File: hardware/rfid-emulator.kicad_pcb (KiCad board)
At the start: 4 copper layers, 162 x 72 mm, 94 parts, among them J1 AVR-JTAG-10, J2 Micro_USB, J3 OSTTC020162, Q1 2N3904, Q2 2N3906, Q3 2N3906, Q4 IRLML6344TRPBF, Q5 IRLML6344TRPBF, SW1 EN11-HSM1BF20, U1 NHD-C0216CiZ-FSW-FBW-3V3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

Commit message: Re-add Noelle's changes
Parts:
- added C32: 1.5n, Capacitors_SMD:C_0805_HandSoldering, F.Cu at (122.0, 81.2)

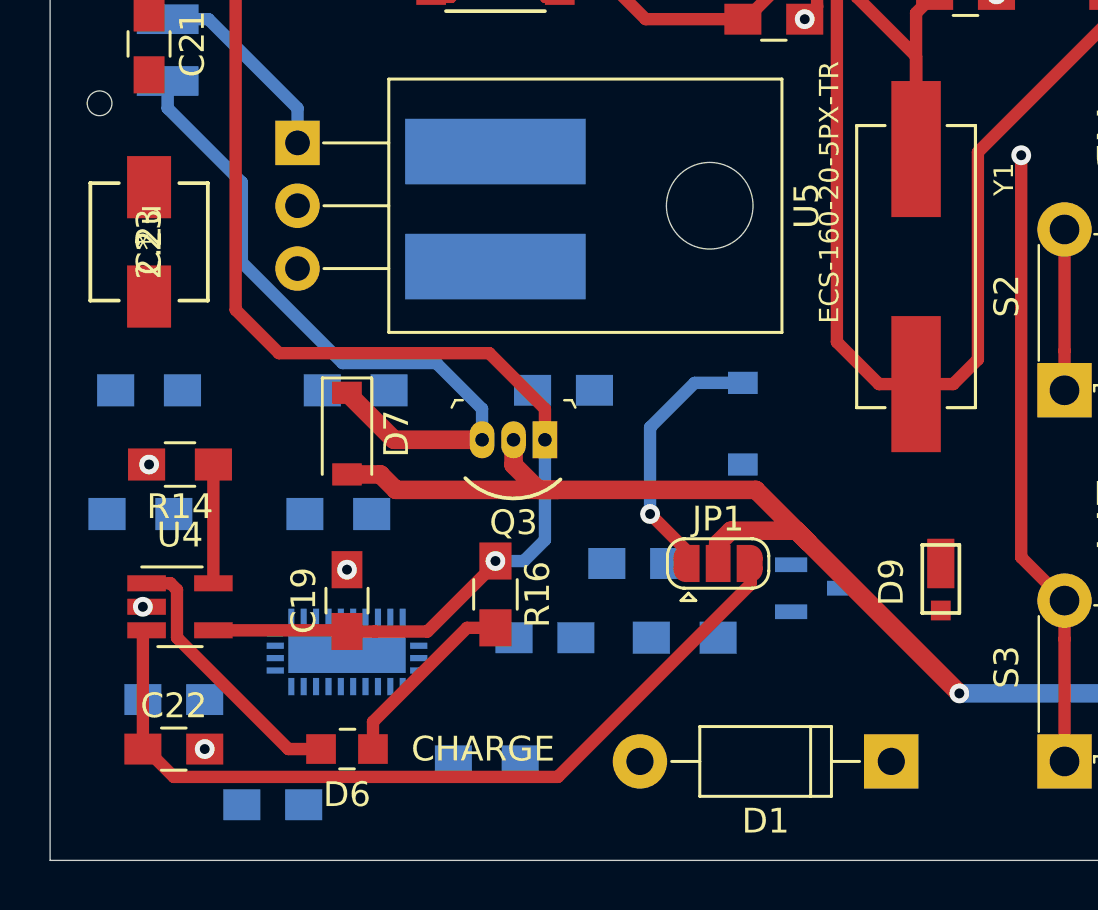
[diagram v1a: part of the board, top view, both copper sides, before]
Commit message: Ian changes rfid-emulator.kicad_pcb
Added all traces and connections associated with the battery management system.
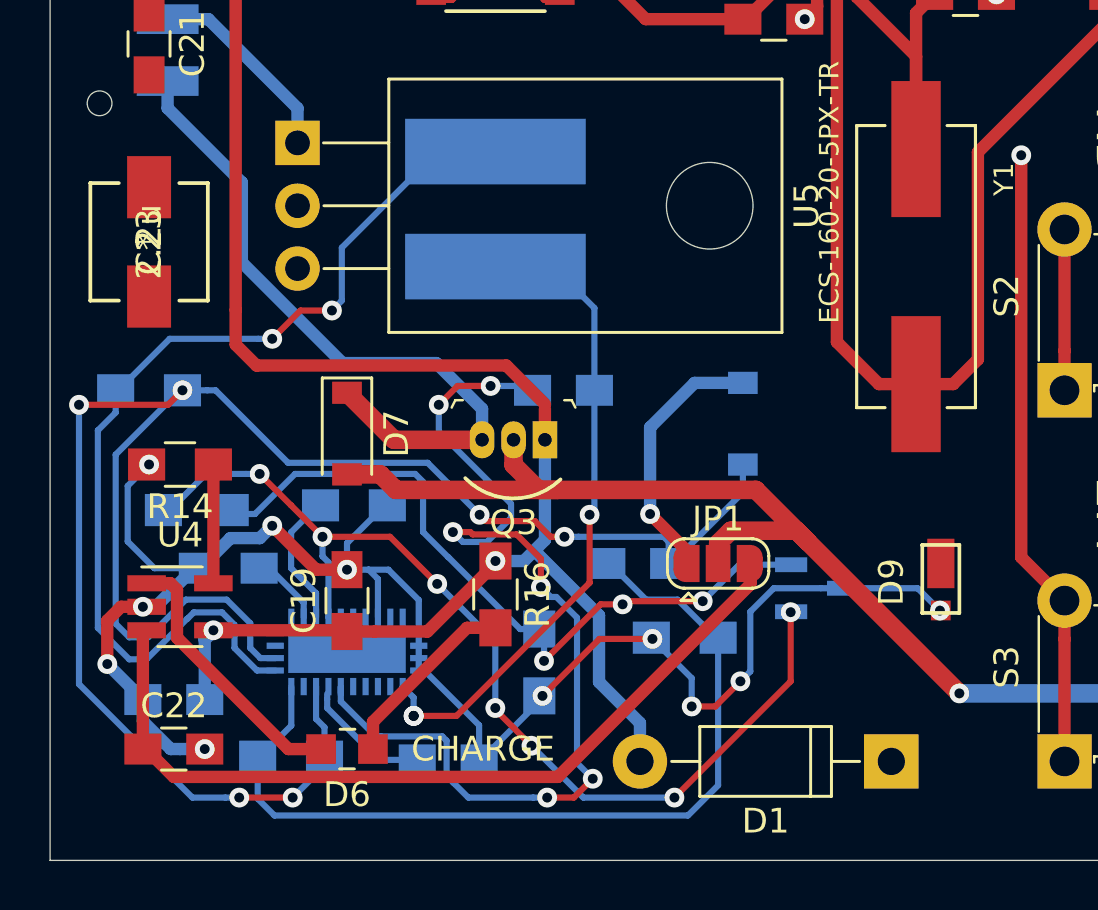
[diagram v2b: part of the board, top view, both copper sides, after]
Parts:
- moved R5 15.0 mm to (78.7, 130.8)
- moved C7 13.1 mm to (76.2, 123.2)
- moved R4 11.7 mm to (81.3, 120.7)
- moved R2 10.1 mm to (88.8, 127.0), turned to 270 degrees
- moved C6 7.32 mm to (85.1, 130.9), turned to 0 degrees
- moved R1 2.29 mm to (74.9, 120.8)
- turned C11 to 180 degrees
- turned R8 to 180 degrees
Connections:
- U2 pad 12: (no net) -> GND
- U2 pad 13: (no net) -> GND
- U2 pad 14: (no net) -> GND
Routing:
- net Net-(C11-Pad1): track 0.00 -> 79.5 mm, vias 0 -> 6
- net GND: track 24.8 -> 94.1 mm, vias 22 -> 29
- net Net-(D1-Pad1): track 0.00 -> 41.6 mm, vias 0 -> 7
- net Net-(C10-Pad1): track 0.00 -> 40.7 mm, vias 0 -> 6
- net Net-(L1-Pad1): track 0.00 -> 40.6 mm, vias 0 -> 2
- net Net-(C11-Pad2): track 0.00 -> 36.3 mm
- net Net-(R1-Pad2): track 0.00 -> 30.0 mm, vias 0 -> 3
- net Net-(C10-Pad2): track 0.00 -> 26.6 mm, vias 0 -> 3
- net /USB_VBUS: track 61.6 -> 75.8 mm, vias 1 -> 2
- net Net-(R4-Pad1): track 0.00 -> 5.49 mm
- net Net-(C6-Pad1): track 0.00 -> 5.08 mm
- net Net-(C7-Pad2): track 0.00 -> 2.97 mm

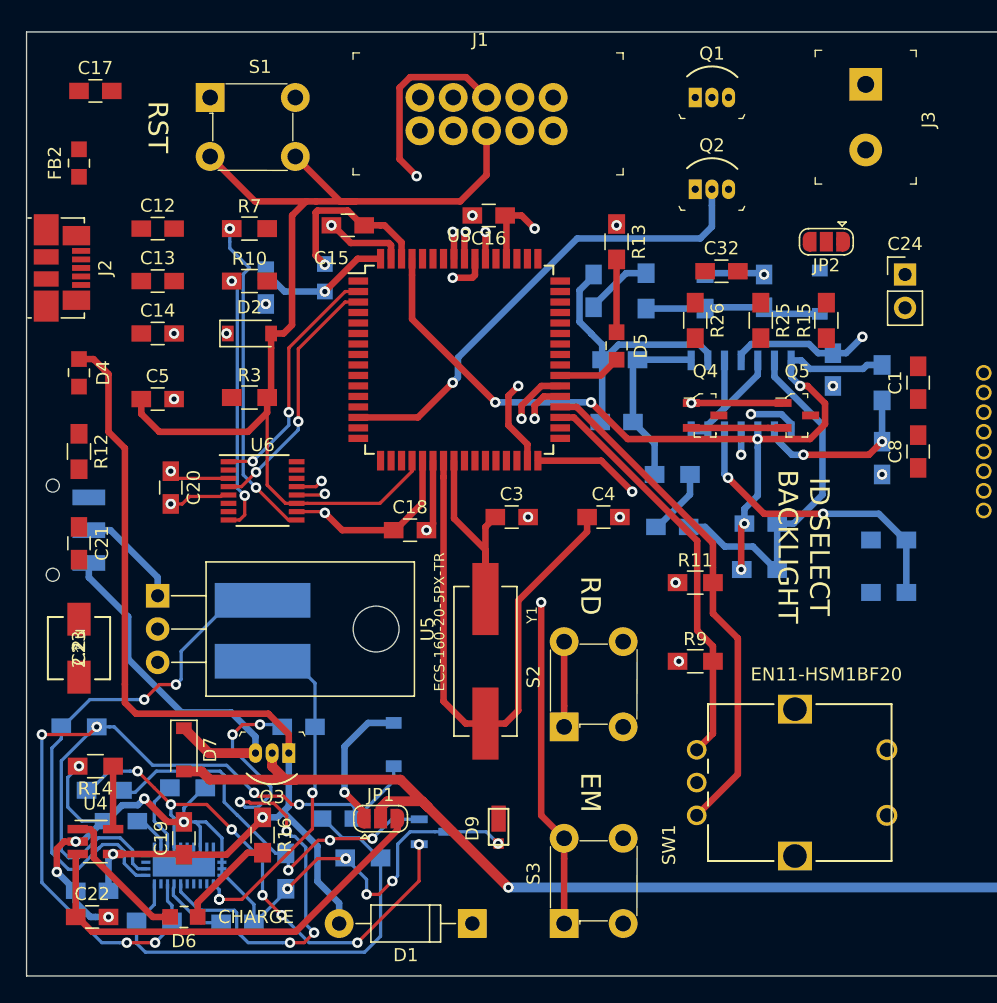
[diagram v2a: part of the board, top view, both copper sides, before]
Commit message: Delete extraneous traces and modify some problematic footprints
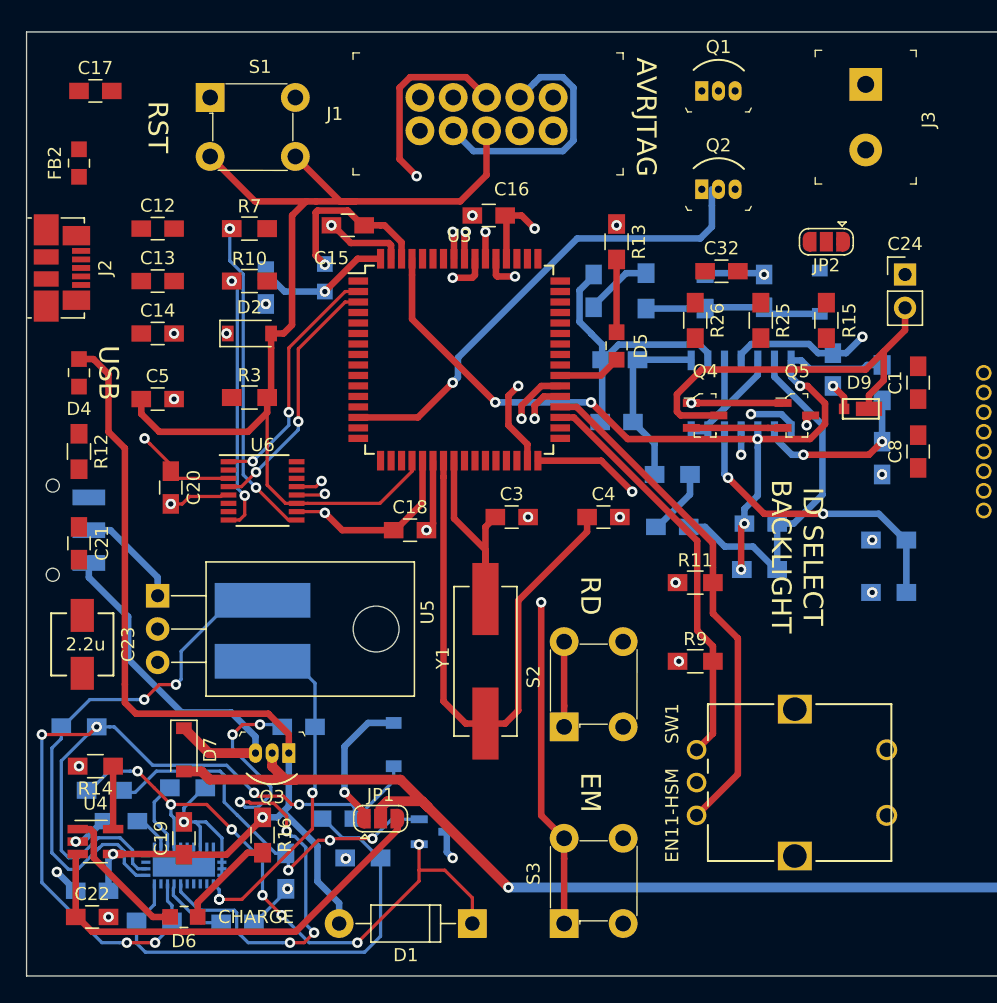
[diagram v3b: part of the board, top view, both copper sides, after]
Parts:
- SW1: value EN11-HSM1BF20 -> EN11-HSM
- moved D9 42.1 mm to (133.2, 91.8), turned to 180 degrees
- moved Q1 0.71 mm to (120.5, 67.5)
- moved SW1 0.57 mm to (127.5, 120.2)
- moved Q2 0.50 mm to (120.5, 75.0)
- moved C23 0.38 mm to (73.2, 109.7)
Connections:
- U2 pad 12: GND -> (no net)
- U2 pad 13: GND -> (no net)
- U2 pad 14: GND -> (no net)
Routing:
- net GND: track 94.1 -> 53.0 mm
- net /ANTENNA: track 0.00 -> 30.6 mm
- net +3V3: track 51.1 -> 73.6 mm, vias 10 -> 11
- net Net-(D1-Pad1): track 41.6 -> 48.5 mm
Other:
- board text added: "AVRJTAG"
- board text added: "OFF"
- board text added: "ON"
- board text added: "USB"

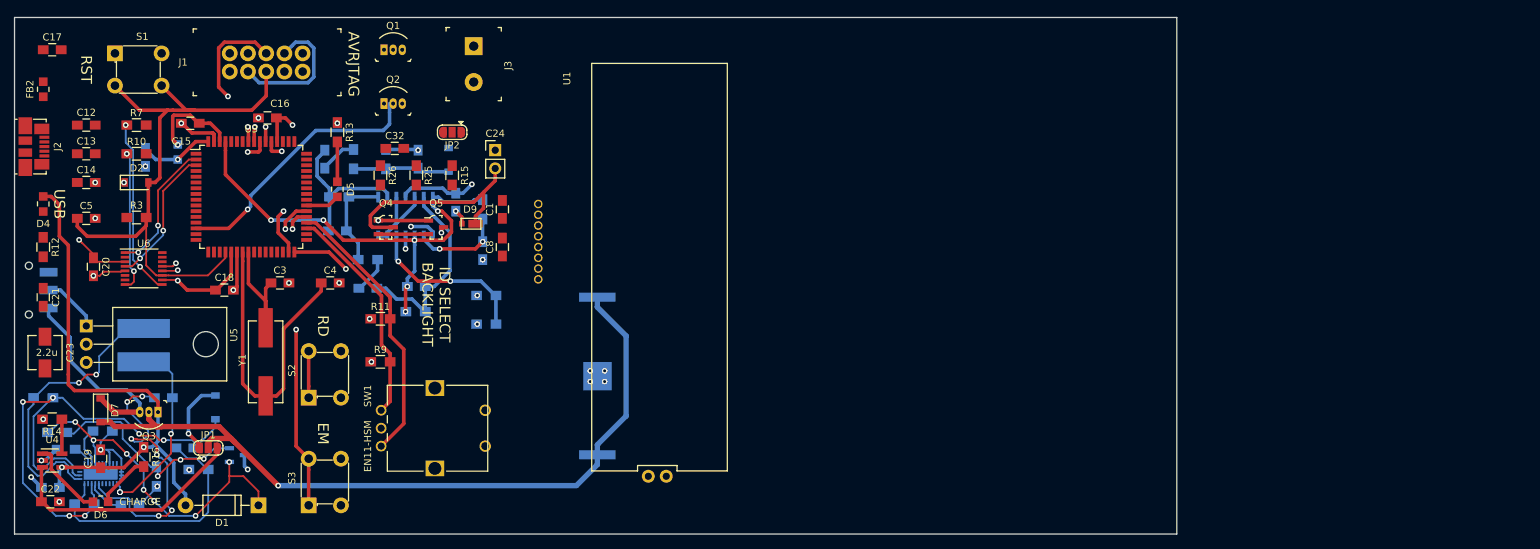
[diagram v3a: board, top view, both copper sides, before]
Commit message: Finished driver and added antenna
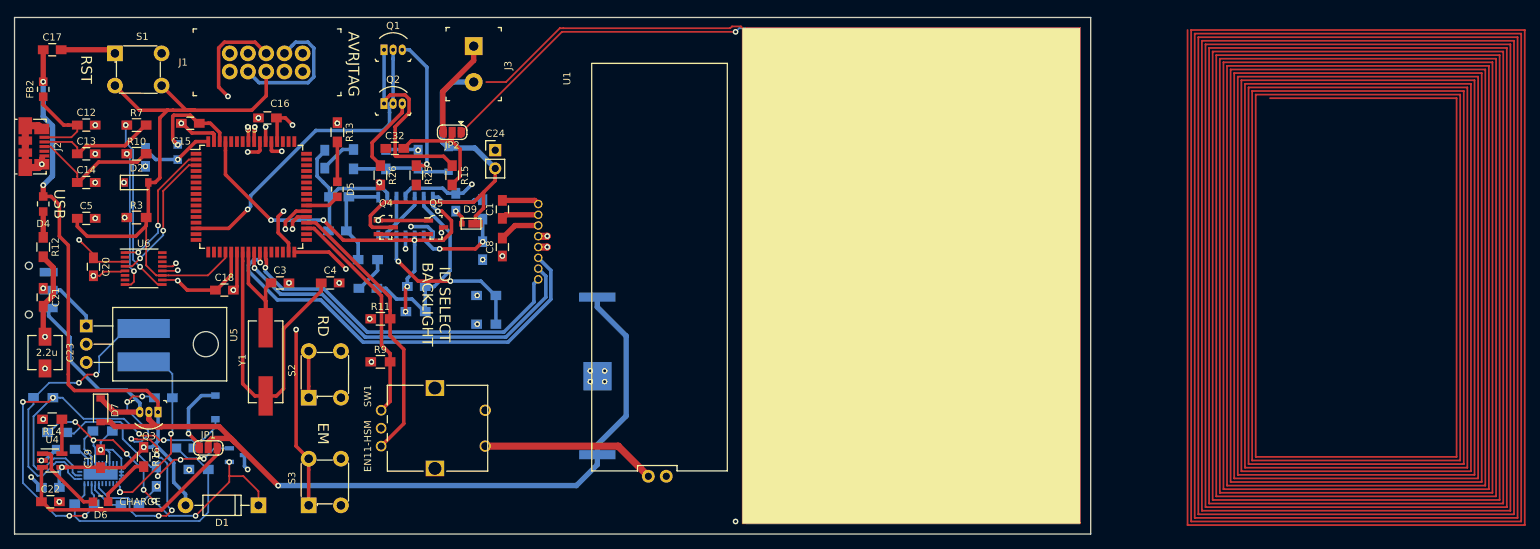
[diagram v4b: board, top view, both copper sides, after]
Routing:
- net (no net): track 0.00 -> 23319.6 mm, vias 0 -> 4
- net /I2C_SDA: track 0.00 -> 59.7 mm, vias 0 -> 1
- net /I2C_SCL: track 0.00 -> 53.6 mm, vias 0 -> 1
- net /~I2C_RST~: track 0.00 -> 48.9 mm, vias 0 -> 1
- net GND: track 53.0 -> 86.6 mm, vias 29 -> 35
- net Net-(Q1-Pad1): track 0.00 -> 29.2 mm
- net /BKL_SW2: track 0.00 -> 24.5 mm
- net /USB_VBUS: track 75.8 -> 97.3 mm, vias 2 -> 4
- net /ANTENNA: track 30.6 -> 51.4 mm
- net Net-(Q1-Pad3): track 0.00 -> 19.5 mm, vias 0 -> 1
- net Net-(C14-Pad1): track 0.00 -> 18.7 mm
- net Net-(C13-Pad1): track 0.00 -> 17.0 mm
- net Net-(C32-Pad2): track 0.00 -> 16.3 mm
- net Net-(J3-Pad1): track 0.00 -> 13.8 mm
- net Net-(C12-Pad1): track 0.00 -> 12.8 mm
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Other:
- board size 162 x 72 mm -> 150 x 72 mm
- board text removed: "Rough outline of antenna area"

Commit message: Fix most DRC failures on PCB check
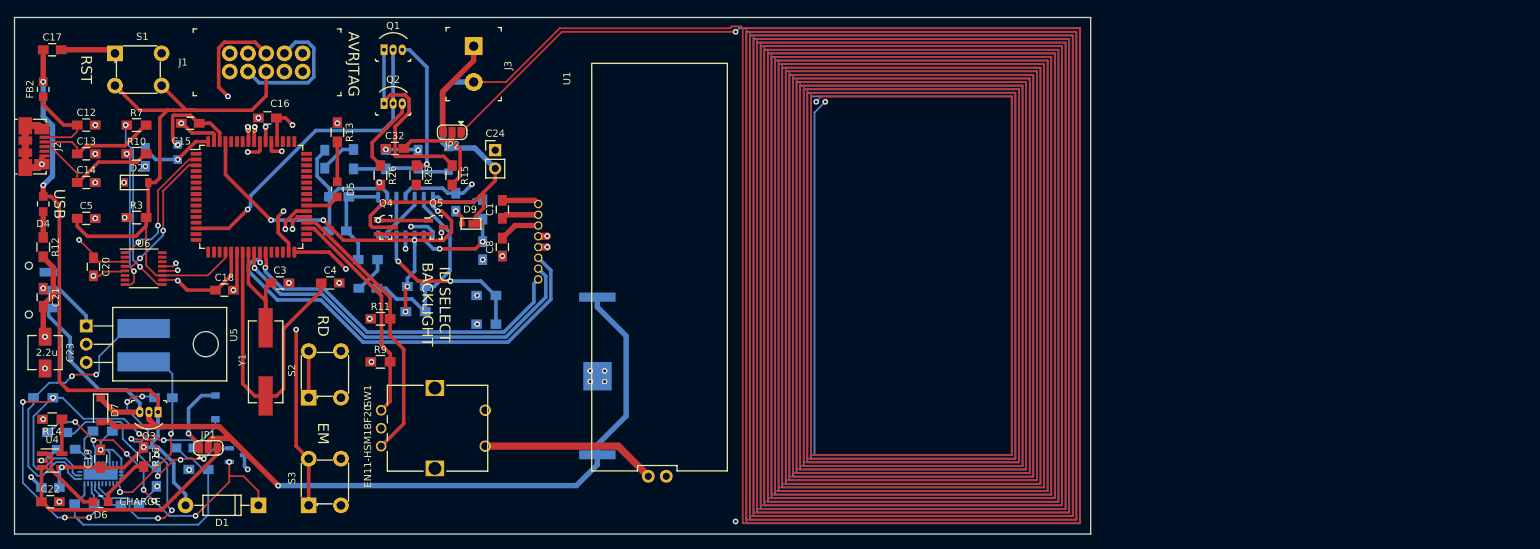
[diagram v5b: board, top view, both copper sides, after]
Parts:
- SW1: value EN11-HSM -> EN11-HSM1BF20
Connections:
- J1 pad 8: (no net) -> Net-(J1-Pad8)
- J2 pad 4: (no net) -> Net-(J2-Pad4)
- JP2 pad 1: (no net) -> /ANTENNA
- R25 pad 2: (no net) -> +5V
- S4 pad 3: (no net) -> Net-(S4-Pad3)
- U2 pad 1: (no net) -> Net-(U2-Pad1)
- U2 pad 23: (no net) -> Net-(U2-Pad23)
- U2 pad 27: (no net) -> Net-(U2-Pad27)
- U2 pad 28: (no net) -> Net-(U2-Pad28)
- U3 pad 1: (no net) -> Net-(U3-Pad1)
- U3 pad 10: (no net) -> Net-(U3-Pad10)
- U3 pad 11: (no net) -> Net-(U3-Pad11)
- U3 pad 12: (no net) -> Net-(U3-Pad12)
- U3 pad 13: (no net) -> Net-(U3-Pad13)
- U3 pad 15: (no net) -> Net-(U3-Pad15)
- U3 pad 16: (no net) -> Net-(U3-Pad16)
- U3 pad 17: (no net) -> Net-(U3-Pad17)
- U3 pad 18: (no net) -> Net-(U3-Pad18)
- U3 pad 19: (no net) -> Net-(U3-Pad19)
- U3 pad 28: (no net) -> Net-(U3-Pad28)
- U3 pad 29: (no net) -> Net-(U3-Pad29)
- U3 pad 30: (no net) -> Net-(U3-Pad30)
- U3 pad 33: (no net) -> Net-(U3-Pad33)
- U3 pad 34: (no net) -> Net-(U3-Pad34)
- U3 pad 4: (no net) -> Net-(U3-Pad4)
- U3 pad 40: (no net) -> Net-(U3-Pad40)
- U3 pad 41: (no net) -> Net-(U3-Pad41)
- U3 pad 42: (no net) -> Net-(U3-Pad42)
- U3 pad 43: (no net) -> Net-(U3-Pad43)
- U3 pad 44: (no net) -> Net-(U3-Pad44)
- U3 pad 45: (no net) -> Net-(U3-Pad45)
- U3 pad 46: (no net) -> Net-(U3-Pad46)
- U3 pad 47: (no net) -> Net-(U3-Pad47)
- U3 pad 48: (no net) -> Net-(U3-Pad48)
- U3 pad 49: (no net) -> Net-(U3-Pad49)
- U3 pad 5: (no net) -> Net-(U3-Pad5)
- U3 pad 50: (no net) -> Net-(U3-Pad50)
- U3 pad 51: (no net) -> Net-(U3-Pad51)
- U3 pad 58: (no net) -> Net-(U3-Pad58)
- U3 pad 59: (no net) -> Net-(U3-Pad59)
- U3 pad 6: (no net) -> Net-(U3-Pad6)
- U3 pad 60: (no net) -> Net-(U3-Pad60)
- U3 pad 7: (no net) -> Net-(U3-Pad7)
- U3 pad 8: (no net) -> Net-(U3-Pad8)
- U3 pad 9: (no net) -> Net-(U3-Pad9)
- U6 pad 14: (no net) -> Net-(U6-Pad14)
- U6 pad 15: (no net) -> Net-(U6-Pad15)
- U6 pad 16: (no net) -> Net-(U6-Pad16)
- U6 pad 2: (no net) -> Net-(U6-Pad2)
- U6 pad 6: (no net) -> Net-(U6-Pad6)
- U6 pad 7: (no net) -> Net-(U6-Pad7)
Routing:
- net (no net): track 23319.6 -> 0.00 mm, vias 4 -> 0
- net /ANTENNA: track 51.4 -> 15616.8 mm, vias 0 -> 4
- net Net-(C11-Pad1): track 79.5 -> 80.8 mm
- net /USB_VBUS: track 97.3 -> 98.3 mm
- net Net-(C11-Pad2): track 36.3 -> 37.2 mm
- net GND: vias 35 -> 36

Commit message: Add test points and extra capacitor socket
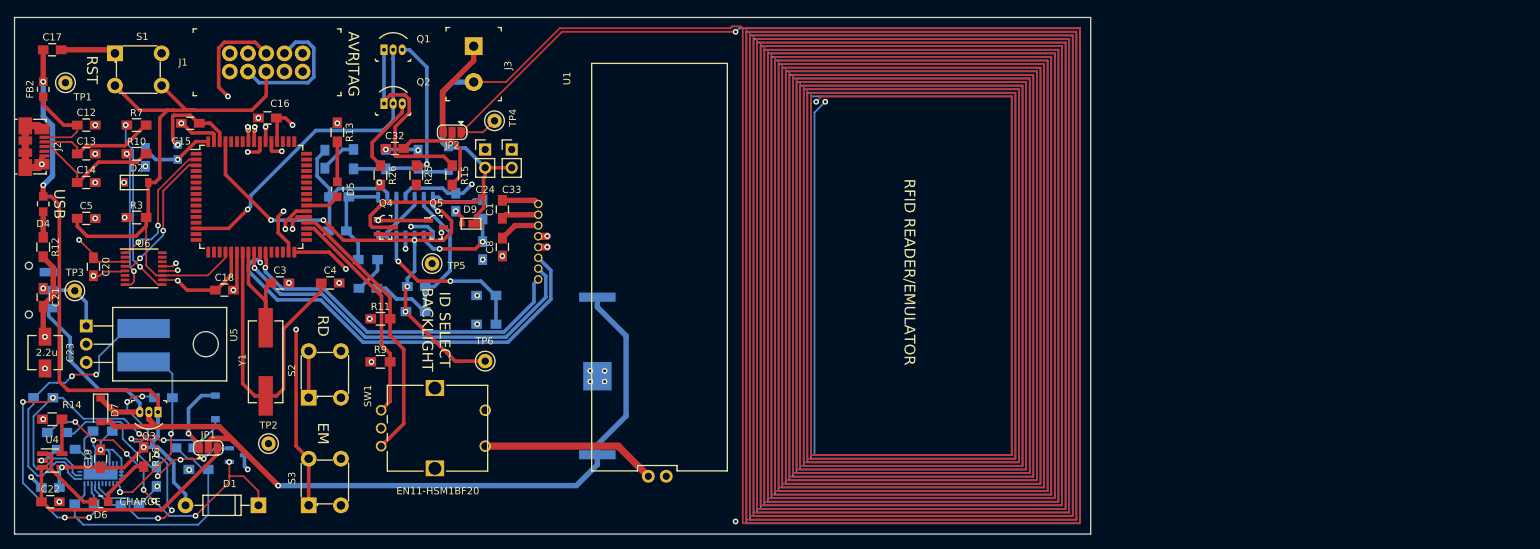
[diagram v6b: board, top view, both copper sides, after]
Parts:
- added C33: 0.0n, Socket_Strips:Socket_Strip_Straight_1x02_Pitch2.54mm, F.Cu at (138.3, 81.4)
- added TP1: 5001, digikey-footprints:Test_Point_D1.02mm, F.Cu at (76.1, 72.1)
- added TP2: 5000, digikey-footprints:Test_Point_D1.02mm, F.Cu at (104.4, 122.4)
- added TP3: 5000, digikey-footprints:Test_Point_D1.02mm, F.Cu at (77.4, 101.1)
- added TP4: 5002, digikey-footprints:Test_Point_D1.02mm, F.Cu at (135.9, 77.4)
- added TP5: 5002, digikey-footprints:Test_Point_D1.02mm, F.Cu at (127.2, 97.3)
- added TP6: 5002, digikey-footprints:Test_Point_D1.02mm, F.Cu at (134.6, 110.9)
- moved C24 1.40 mm to (134.6, 81.4)
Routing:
- net /DATA_IN_AN: track 65.0 -> 79.0 mm
- net /DATA_OUT: track 25.3 -> 35.6 mm
- net /ANTENNA: track 15616.8 -> 15623.7 mm
- net /VSUPPLY: track 8.14 -> 9.25 mm
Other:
- board text added: "RFID READER/EMULATOR"
